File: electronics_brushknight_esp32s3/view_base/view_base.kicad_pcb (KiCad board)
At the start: 4 copper layers, 81.2 x 81.2 mm, 108 parts, among them J1 BLDC, J2 USB_C_Receptacle_USB2.0, J3 LCD, J4 A, J5 B, J6 LCD - FPC, Q1 MMBT4403, Q2 UMH3N, U1 MT6701-CT, U10 ESP32-S3-WROOM-1-N8R8, U2 CP2102N-A02-GQFN28, U4 HX711, U5 TMC6300, U7 SN74LV1T34DBV, U8 VEML7700, U9 TS1117BCW33_RPG

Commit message: re-routed things
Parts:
- removed D1, D2, D3, D4, D5, D6, D7, D8: SK6812SIDE-A, cleaned footprints:SK6812-SIDE-A
- removed H4: MountHole, Holes:MountingHole_2.2mm_M2_ISO7380_Pad_NonVirtual
- removed Q2: UMH3N, cleaned footprints:SOT-363_SC-70-6
- removed R22: 1K, cleaned footprints:R_0603_1608Metric
- added C100: 0.1uF, cleaned footprints:C_0402_1005Metric, F.Cu at (89.3, 122.8)
- added C101: 0.1uF, cleaned footprints:C_0402_1005Metric, F.Cu at (93.5, 124.3)
- added C11: 0.1uF, cleaned footprints:C_0402_1005Metric, F.Cu at (125.1, 97.8)
- added C30: 0.1uF, cleaned footprints:C_0402_1005Metric, F.Cu at (100.0, 125.2)
- added C31: 0.1uF, cleaned footprints:C_0402_1005Metric, F.Cu at (97.8, 74.9)
- added C32: 0.1uF, cleaned footprints:C_0402_1005Metric, F.Cu at (97.8, 125.1)
- added C33: 0.1uF, cleaned footprints:C_0402_1005Metric, F.Cu at (102.2, 74.9)
- added C34: 0.1uF, cleaned footprints:C_0402_1005Metric, F.Cu at (106.5, 124.3)
- added C35: 0.1uF, cleaned footprints:C_0402_1005Metric, F.Cu at (100.0, 74.8)
- added C36: 0.1uF, cleaned footprints:C_0402_1005Metric, F.Cu at (110.7, 122.9)
- added C37: 0.1uF, cleaned footprints:C_0402_1005Metric, F.Cu at (108.6, 76.3)
- added C38: 0.1uF, cleaned footprints:C_0402_1005Metric, F.Cu at (112.6, 78.2)
- added C39: 0.1uF, cleaned footprints:C_0402_1005Metric, F.Cu at (114.5, 120.7)
- added C40: 0.1uF, cleaned footprints:C_0402_1005Metric, F.Cu at (116.2, 80.7)
- added C41: 0.1uF, cleaned footprints:C_0402_1005Metric, F.Cu at (117.8, 117.8)
- added C42: 0.1uF, cleaned footprints:C_0402_1005Metric, F.Cu at (119.3, 83.8)
- added C43: 0.1uF, cleaned footprints:C_0402_1005Metric, F.Cu at (120.7, 114.5)
- added C44: 0.1uF, cleaned footprints:C_0402_1005Metric, F.Cu at (121.8, 87.4)
- added C45: 0.1uF, cleaned footprints:C_0402_1005Metric, F.Cu at (123.7, 91.4)
- added C46: 0.1uF, cleaned footprints:C_0402_1005Metric, F.Cu at (122.8, 110.7)
- added C47: 0.1uF, cleaned footprints:C_0402_1005Metric, F.Cu at (91.4, 76.3)
- added C48: 0.1uF, cleaned footprints:C_0402_1005Metric, F.Cu at (124.3, 106.5)
- added C49: 0.1uF, cleaned footprints:C_0402_1005Metric, F.Cu at (87.4, 78.2)
- added C50: 0.1uF, cleaned footprints:C_0402_1005Metric, F.Cu at (124.8, 104.4)
- added C51: 0.1uF, cleaned footprints:C_0402_1005Metric, F.Cu at (83.8, 80.7)
- added C52: 0.1uF, cleaned footprints:C_0402_1005Metric, F.Cu at (80.7, 83.8)
- added C53: 0.1uF, cleaned footprints:C_0402_1005Metric, F.Cu at (124.3, 93.5)
- added C54: 0.1uF, cleaned footprints:C_0402_1005Metric, F.Cu at (78.2, 87.4)
- added C55: 0.1uF, cleaned footprints:C_0402_1005Metric, F.Cu at (124.8, 95.6)
- added C56: 0.1uF, cleaned footprints:C_0402_1005Metric, F.Cu at (76.3, 91.4)
- added C57: 0.1uF, cleaned footprints:C_0402_1005Metric, F.Cu at (122.8, 89.3)
- added C58: 0.1uF, cleaned footprints:C_0402_1005Metric, F.Cu at (74.9, 97.8)
- added C59: 0.1uF, cleaned footprints:C_0402_1005Metric, F.Cu at (74.9, 102.2)
- added C60: 0.1uF, cleaned footprints:C_0402_1005Metric, F.Cu at (74.8, 100.0)
- added C61: 0.1uF, cleaned footprints:C_0402_1005Metric, F.Cu at (76.3, 108.6)
- added C62: 0.1uF, cleaned footprints:C_0402_1005Metric, F.Cu at (78.2, 112.6)
- added C63: 0.1uF, cleaned footprints:C_0402_1005Metric, F.Cu at (120.7, 85.5)
- added C64: 0.1uF, cleaned footprints:C_0402_1005Metric, F.Cu at (117.8, 82.2)
- added C65: 0.1uF, cleaned footprints:C_0402_1005Metric, F.Cu at (114.5, 79.3)
- added C66: 0.1uF, cleaned footprints:C_0402_1005Metric, F.Cu at (110.7, 77.2)
- added C67: 0.1uF, cleaned footprints:C_0402_1005Metric, F.Cu at (80.7, 116.2)
- added C68: 0.1uF, cleaned footprints:C_0402_1005Metric, F.Cu at (83.8, 119.3)
- added C69: 0.1uF, cleaned footprints:C_0402_1005Metric, F.Cu at (87.4, 121.8)
- added C70: 0.1uF, cleaned footprints:C_0402_1005Metric, F.Cu at (91.4, 123.7)
- added C71: 0.1uF, cleaned footprints:C_0402_1005Metric, F.Cu at (106.5, 75.6)
- added C72: 0.1uF, cleaned footprints:C_0402_1005Metric, F.Cu at (104.4, 75.2)
- added C73: 0.1uF, cleaned footprints:C_0402_1005Metric, F.Cu at (93.5, 75.6)
- added C74: 0.1uF, cleaned footprints:C_0402_1005Metric, F.Cu at (95.6, 75.2)
- added C75: 0.1uF, cleaned footprints:C_0402_1005Metric, F.Cu at (95.6, 124.8)
- added C76: 0.1uF, cleaned footprints:C_0402_1005Metric, F.Cu at (102.2, 125.1)
- added C77: 0.1uF, cleaned footprints:C_0402_1005Metric, F.Cu at (104.4, 124.8)
- added C79: 0.1uF, cleaned footprints:C_0402_1005Metric, F.Cu at (89.3, 77.2)
- added C80: 0.1uF, cleaned footprints:C_0402_1005Metric, F.Cu at (85.5, 79.4)
- added C81: 0.1uF, cleaned footprints:C_0402_1005Metric, F.Cu at (82.2, 82.2)
- added C82: 0.1uF, cleaned footprints:C_0402_1005Metric, F.Cu at (79.4, 85.5)
- added C88: 0.1uF, cleaned footprints:C_0402_1005Metric, F.Cu at (77.2, 89.3)
- added C90: 0.1uF, cleaned footprints:C_0402_1005Metric, F.Cu at (75.7, 93.5)
- added C92: 0.1uF, cleaned footprints:C_0402_1005Metric, F.Cu at (75.2, 95.6)
- added C94: 0.1uF, cleaned footprints:C_0402_1005Metric, F.Cu at (75.2, 104.4)
- added C95: 0.1uF, cleaned footprints:C_0402_1005Metric, F.Cu at (75.6, 106.5)
- added C96: 0.1uF, cleaned footprints:C_0402_1005Metric, F.Cu at (77.2, 110.7)
- added C97: 0.1uF, cleaned footprints:C_0402_1005Metric, F.Cu at (79.3, 114.5)
- added C98: 0.1uF, cleaned footprints:C_0402_1005Metric, F.Cu at (82.2, 117.8)
- added C99: 0.1uF, cleaned footprints:C_0402_1005Metric, F.Cu at (85.5, 120.6)
- added D10: SK6812, cleaned footprints:LED_SK6812_EC15_1.5x1.5mm, F.Cu at (97.7, 126.7)
- added D11: SK6812, cleaned footprints:LED_SK6812_EC15_1.5x1.5mm, F.Cu at (95.3, 126.3)
- added D12: SK6812, cleaned footprints:LED_SK6812_EC15_1.5x1.5mm, F.Cu at (93.1, 125.8)
- added D13: SK6812, cleaned footprints:LED_SK6812_EC15_1.5x1.5mm, F.Cu at (90.8, 125.1)
- added D14: SK6812, cleaned footprints:LED_SK6812_EC15_1.5x1.5mm, F.Cu at (88.7, 124.2)
- added D15: SK6812, cleaned footprints:LED_SK6812_EC15_1.5x1.5mm, F.Cu at (86.6, 123.2)
- added D16: SK6812, cleaned footprints:LED_SK6812_EC15_1.5x1.5mm, F.Cu at (84.7, 121.9)
- added D17: SK6812, cleaned footprints:LED_SK6812_EC15_1.5x1.5mm, F.Cu at (82.8, 120.5)
- added D18: SK6812, cleaned footprints:LED_SK6812_EC15_1.5x1.5mm, F.Cu at (81.1, 118.9)
- added D19: SK6812, cleaned footprints:LED_SK6812_EC15_1.5x1.5mm, F.Cu at (79.5, 117.2)
- added D20: SK6812, cleaned footprints:LED_SK6812_EC15_1.5x1.5mm, F.Cu at (78.1, 115.3)
- added D21: SK6812, cleaned footprints:LED_SK6812_EC15_1.5x1.5mm, F.Cu at (76.8, 113.4)
- added D22: SK6812, cleaned footprints:LED_SK6812_EC15_1.5x1.5mm, F.Cu at (75.8, 111.3)
- added D23: SK6812, cleaned footprints:LED_SK6812_EC15_1.5x1.5mm, F.Cu at (74.9, 109.2)
- added D24: SK6812, cleaned footprints:LED_SK6812_EC15_1.5x1.5mm, F.Cu at (74.2, 106.9)
- added D25: SK6812, cleaned footprints:LED_SK6812_EC15_1.5x1.5mm, F.Cu at (73.7, 104.6)
- added D26: SK6812, cleaned footprints:LED_SK6812_EC15_1.5x1.5mm, F.Cu at (73.4, 102.3)
- added D27: SK6812, cleaned footprints:LED_SK6812_EC15_1.5x1.5mm, F.Cu at (73.2, 100.0)
- added D28: SK6812, cleaned footprints:LED_SK6812_EC15_1.5x1.5mm, F.Cu at (73.4, 97.7)
- added D29: SK6812, cleaned footprints:LED_SK6812_EC15_1.5x1.5mm, F.Cu at (73.7, 95.4)
- added D30: SK6812, cleaned footprints:LED_SK6812_EC15_1.5x1.5mm, F.Cu at (74.2, 93.1)
- added D31: SK6812, cleaned footprints:LED_SK6812_EC15_1.5x1.5mm, F.Cu at (74.9, 90.9)
- added D32: SK6812, cleaned footprints:LED_SK6812_EC15_1.5x1.5mm, F.Cu at (75.8, 88.7)
- added D33: SK6812, cleaned footprints:LED_SK6812_EC15_1.5x1.5mm, F.Cu at (76.8, 86.6)
- added D34: SK6812, cleaned footprints:LED_SK6812_EC15_1.5x1.5mm, F.Cu at (78.1, 84.7)
- added D35: SK6812, cleaned footprints:LED_SK6812_EC15_1.5x1.5mm, F.Cu at (79.5, 82.8)
- added D36: SK6812, cleaned footprints:LED_SK6812_EC15_1.5x1.5mm, F.Cu at (81.1, 81.1)
- added D37: SK6812, cleaned footprints:LED_SK6812_EC15_1.5x1.5mm, F.Cu at (82.8, 79.5)
- added D38: SK6812, cleaned footprints:LED_SK6812_EC15_1.5x1.5mm, F.Cu at (84.7, 78.1)
- added D39: SK6812, cleaned footprints:LED_SK6812_EC15_1.5x1.5mm, F.Cu at (86.6, 76.8)
- added D40: SK6812, cleaned footprints:LED_SK6812_EC15_1.5x1.5mm, F.Cu at (88.7, 75.8)
- added D41: SK6812, cleaned footprints:LED_SK6812_EC15_1.5x1.5mm, F.Cu at (90.8, 74.9)
- added D42: SK6812, cleaned footprints:LED_SK6812_EC15_1.5x1.5mm, F.Cu at (109.2, 74.9)
- added D43: SK6812, cleaned footprints:LED_SK6812_EC15_1.5x1.5mm, F.Cu at (123.2, 86.6)
- added D44: SK6812, cleaned footprints:LED_SK6812_EC15_1.5x1.5mm, F.Cu at (126.3, 104.6)
- added D45: SK6812, cleaned footprints:LED_SK6812_EC15_1.5x1.5mm, F.Cu at (93.1, 74.2)
- added D46: SK6812, cleaned footprints:LED_SK6812_EC15_1.5x1.5mm, F.Cu at (111.3, 75.8)
- added D47: SK6812, cleaned footprints:LED_SK6812_EC15_1.5x1.5mm, F.Cu at (124.2, 88.7)
- added D48: SK6812, cleaned footprints:LED_SK6812_EC15_1.5x1.5mm, F.Cu at (125.8, 106.9)
- added D49: SK6812, cleaned footprints:LED_SK6812_EC15_1.5x1.5mm, F.Cu at (95.4, 73.7)
- added D50: SK6812, cleaned footprints:LED_SK6812_EC15_1.5x1.5mm, F.Cu at (113.4, 76.8)
- added D51: SK6812, cleaned footprints:LED_SK6812_EC15_1.5x1.5mm, F.Cu at (125.1, 90.9)
- added D52: SK6812, cleaned footprints:LED_SK6812_EC15_1.5x1.5mm, F.Cu at (125.1, 109.2)
- added D53: SK6812, cleaned footprints:LED_SK6812_EC15_1.5x1.5mm, F.Cu at (97.7, 73.4)
- added D54: SK6812, cleaned footprints:LED_SK6812_EC15_1.5x1.5mm, F.Cu at (115.3, 78.1)
- added D55: SK6812, cleaned footprints:LED_SK6812_EC15_1.5x1.5mm, F.Cu at (125.8, 93.1)
- added D56: SK6812, cleaned footprints:LED_SK6812_EC15_1.5x1.5mm, F.Cu at (124.2, 111.3)
- added D57: SK6812, cleaned footprints:LED_SK6812_EC15_1.5x1.5mm, F.Cu at (100.0, 73.2)
- added D58: SK6812, cleaned footprints:LED_SK6812_EC15_1.5x1.5mm, F.Cu at (117.2, 79.5)
- added D59: SK6812, cleaned footprints:LED_SK6812_EC15_1.5x1.5mm, F.Cu at (126.3, 95.4)
- added D60: SK6812, cleaned footprints:LED_SK6812_EC15_1.5x1.5mm, F.Cu at (123.2, 113.4)
- added D61: SK6812, cleaned footprints:LED_SK6812_EC15_1.5x1.5mm, F.Cu at (102.3, 73.4)
- added D62: SK6812, cleaned footprints:LED_SK6812_EC15_1.5x1.5mm, F.Cu at (118.9, 81.1)
- added D63: SK6812, cleaned footprints:LED_SK6812_EC15_1.5x1.5mm, F.Cu at (126.6, 97.7)
- added D64: SK6812, cleaned footprints:LED_SK6812_EC15_1.5x1.5mm, F.Cu at (121.9, 115.3)
- added D65: SK6812, cleaned footprints:LED_SK6812_EC15_1.5x1.5mm, F.Cu at (104.7, 73.7)
- added D66: SK6812, cleaned footprints:LED_SK6812_EC15_1.5x1.5mm, F.Cu at (120.5, 82.8)
- added D67: SK6812, cleaned footprints:LED_SK6812_EC15_1.5x1.5mm, F.Cu at (126.7, 100.0)
- added D68: SK6812, cleaned footprints:LED_SK6812_EC15_1.5x1.5mm, F.Cu at (120.5, 117.2)
- added D69: SK6812, cleaned footprints:LED_SK6812_EC15_1.5x1.5mm, F.Cu at (106.9, 74.2)
- added D70: SK6812, cleaned footprints:LED_SK6812_EC15_1.5x1.5mm, F.Cu at (121.9, 84.7)
- added D71: SK6812, cleaned footprints:LED_SK6812_EC15_1.5x1.5mm, F.Cu at (126.7, 102.3)
- added D72: SK6812, cleaned footprints:LED_SK6812_EC15_1.5x1.5mm, F.Cu at (118.9, 118.9)
- added D73: SK6812, cleaned footprints:LED_SK6812_EC15_1.5x1.5mm, F.Cu at (117.2, 120.5)
- added D74: SK6812, cleaned footprints:LED_SK6812_EC15_1.5x1.5mm, F.Cu at (115.3, 121.9)
- added D75: SK6812, cleaned footprints:LED_SK6812_EC15_1.5x1.5mm, F.Cu at (113.4, 123.2)
- added D76: SK6812, cleaned footprints:LED_SK6812_EC15_1.5x1.5mm, F.Cu at (111.3, 124.2)
- added D77: SK6812, cleaned footprints:LED_SK6812_EC15_1.5x1.5mm, F.Cu at (109.1, 125.1)
- added D78: SK6812, cleaned footprints:LED_SK6812_EC15_1.5x1.5mm, F.Cu at (106.9, 125.8)
- added D79: SK6812, cleaned footprints:LED_SK6812_EC15_1.5x1.5mm, F.Cu at (104.7, 126.3)
- added D80: SK6812, cleaned footprints:LED_SK6812_EC15_1.5x1.5mm, F.Cu at (102.3, 126.7)
- added D9: SK6812, cleaned footprints:LED_SK6812_EC15_1.5x1.5mm, F.Cu at (100.0, 126.8)
- added REF**: fpc_wire_hole_6mm, view_custom:fpc_wire_hole_6mm, F.Cu at (97.2, 102.8)
- C1, C2, C29, C3, C4, C5, C6, C7, C8: footprint cleaned footprints:C_0603_1608Metric -> cleaned footprints:C_0402_1005Metric
- TP1, TP10, TP11, TP12, TP13, TP14, TP15, TP16, TP3, TP4, TP5, TP6, TP7, TP8, TP9: footprint Modified:TestPoint_Pad_D2.0mm_ValueSilk -> cleaned footprints:TestPoint_Pad_D2.0mm_ValueSilk
- TP2: value 3.3v -> 3V3; footprint Modified:TestPoint_Pad_D2.0mm_ValueSilk -> cleaned footprints:TestPoint_Pad_D2.0mm_ValueSilk
- U2: value CP2102N-A02-GQFN28 -> USBLC6-2SC6; footprint cp2102:Silicon_Labs-CP2102N-A02-GQFN28-IPC_A -> Package_TO_SOT_SMD:SOT-23-6
- moved C8 41.1 mm to (125.1, 102.2), turned to 85 degrees
- moved C7 38.1 mm to (125.2, 100.0), turned to 90 degrees
- moved U7 34.0 mm to (89.6, 136.8)
- moved C29 33.9 mm to (89.6, 134.4), turned to 180 degrees
- moved TP12 29.8 mm to (81.8, 138.2)
- moved C1 26.3 mm to (108.6, 123.7), turned to 20 degrees
- moved C6 26.3 mm to (123.7, 108.6), turned to 70 degrees
- moved TP15 25.8 mm to (65.8, 138.2)
- moved C2 24.2 mm to (112.6, 121.8), turned to 30 degrees
- moved C5 24.2 mm to (121.8, 112.6), turned to 60 degrees
- moved TP14 18.0 mm to (73.8, 138.2), turned to 180 degrees
- moved TP16 14.5 mm to (69.8, 138.2)
- moved TP9 12.7 mm to (67.5, 104.5)
- moved R15 8.63 mm to (67.2, 116.2), turned to -90 degrees
- moved R16 8.63 mm to (68.8, 116.2), turned to 90 degrees
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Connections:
- R13 pad 2: /SDA -> SDA
- R14 pad 2: /SCL -> SCL
- TP4 pad 1: /SDA -> SDA
- TP5 pad 1: /SCL -> SCL
- U10 pad 10: /TMC_VL -> /TMC_WH
- U10 pad 11: /TMC_WL -> /TMC_VH
- U10 pad 12: /SCL -> /TMC_UH
- U10 pad 13: /TMC_UL -> /ESP_USB_D-
- U10 pad 14: /TMC_UH -> /ESP_USB_D+
- U10 pad 18: unconnected-(U10-IO10-Pad18) -> /LCD_RST
- U10 pad 19: unconnected-(U10-IO11-Pad19) -> /MAG_CSN
- U10 pad 20: /TMC_WH -> /LED_DATA_3V3
- U10 pad 22: /MAG_CSN -> /MAG_DO
- U10 pad 23: /TMC_VH -> /STRAIN_DO
- U10 pad 29: /TMC_DIAG -> unconnected-(U10-IO36-Pad29)
- U10 pad 30: /MAG_DO -> unconnected-(U10-IO37-Pad30)
- U10 pad 31: /STRAIN_DO -> SCL
- U10 pad 32: unconnected-(U10-IO39-Pad32) -> SDA
- U10 pad 6: /LCD_RST -> /TMC_DIAG
- U10 pad 7: /LED_DATA_3V3 -> /TMC_VL
- U10 pad 8: /SDA -> /TMC_WL
- U10 pad 9: unconnected-(U10-IO16-Pad9) -> /TMC_UL
- U2 pad 1: unconnected-(U2-DCD-Pad1) -> /USB_D-
- U2 pad 2: unconnected-(U2-~{RI}/CLK-Pad2) -> GND
- U2 pad 3: GND -> /USB_D+
- U2 pad 4: /USB_D+ -> /ESP_USB_D+
- U2 pad 5: /USB_D- -> +5V
- U2 pad 6: +3V3 -> /ESP_USB_D-
- U8 pad 1: /SCL -> SCL
- U8 pad 4: /SDA -> SDA
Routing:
- net /SCL: track 139.1 -> 0.00 mm, vias 3 -> 0
- net SCL: track 0.00 -> 129.3 mm, vias 0 -> 2
- net /SDA: track 128.4 -> 0.00 mm, vias 3 -> 0
- net SDA: track 0.00 -> 115.8 mm, vias 0 -> 2
- net /USB_SERIAL_RXI: track 41.5 -> 9.54 mm
- net /USB_SERIAL_TXO: track 43.5 -> 14.0 mm
- net /ESP32_BOOT: track 56.0 -> 27.7 mm, vias 3 -> 2
- net Net-(D4-DOUT): track 26.0 -> 0.00 mm
- net Net-(D6-DOUT): track 26.0 -> 0.00 mm
- net /MAG_DO: track 79.4 -> 54.0 mm, vias 3 -> 2
- net Net-(D2-DOUT): track 25.3 -> 0.00 mm, vias 2 -> 0
- net /LCD_SCK: track 17.4 -> 40.1 mm, vias 1 -> 2
- net /LCD_CMD: track 7.75 -> 29.7 mm
- net /TMC_DIAG: track 109.5 -> 87.5 mm
- net /LCD_CS: track 23.3 -> 44.3 mm
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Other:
- outline, holes or cut-outs redrawn
- board text added: "SmartKnob DevKit"
- board text added: "esp32s3"
- board text removed: "Base PCB esp32s3"
- board text removed: "SmartKnob View"
- board text removed: "power"

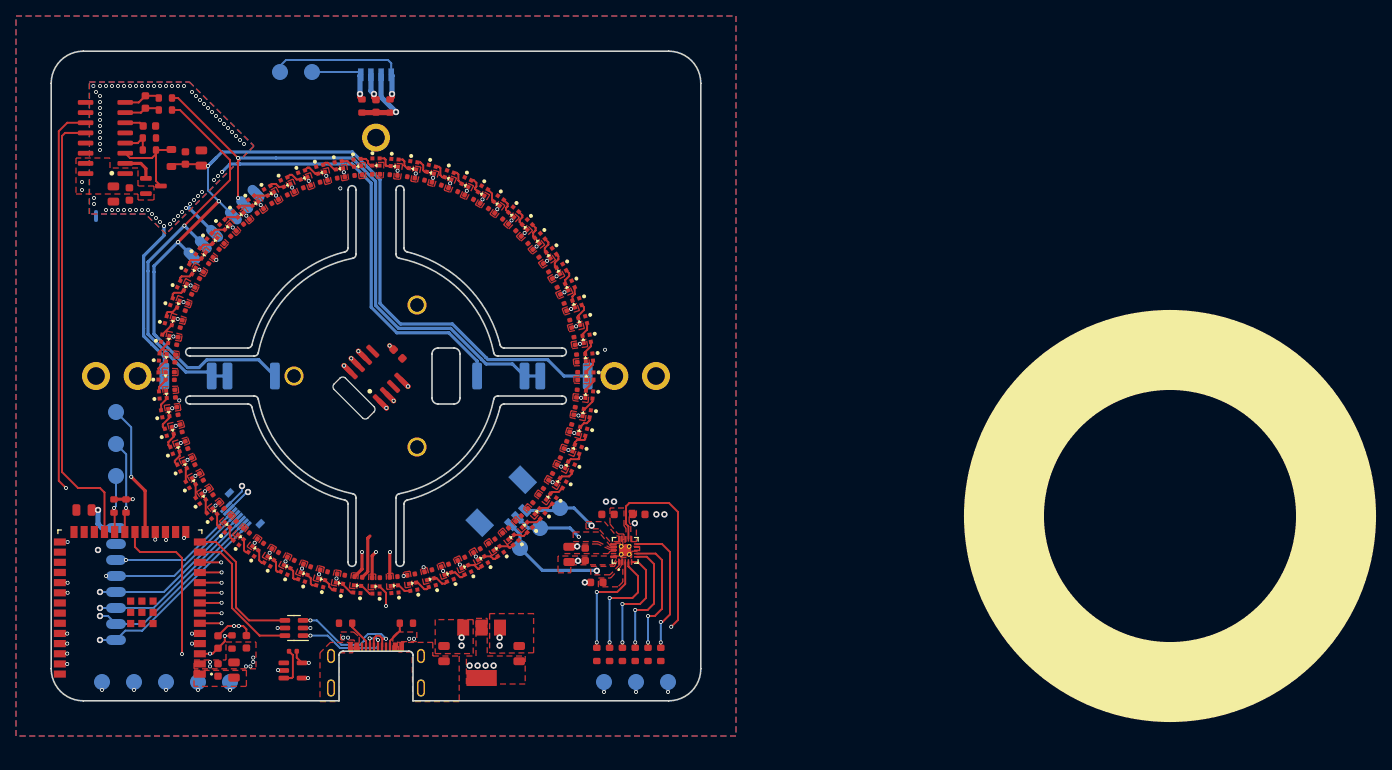
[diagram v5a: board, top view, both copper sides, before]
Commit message: updated screen PCB
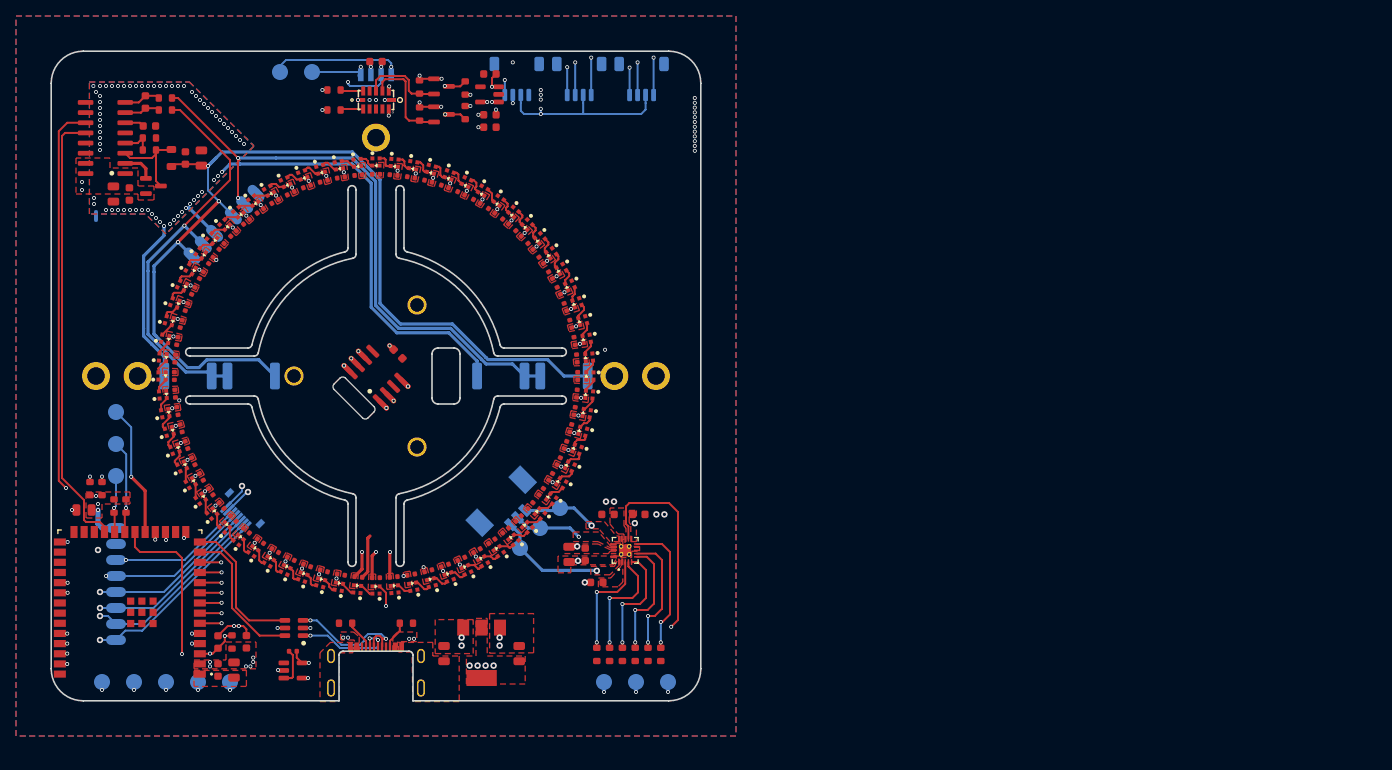
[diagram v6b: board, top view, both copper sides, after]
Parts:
- added C78: 10uF, smd_clean:C_0603_1608Metric, F.Cu at (114.2, 62.2)
- added C83: 10uF, smd_clean:C_0603_1608Metric, F.Cu at (114.2, 67.3)
- added C84: 100nF, smd_clean:C_0603_1608Metric, F.Cu at (114.2, 68.9)
- added J7: Conn_01x04_Socket, cleaned footprints:JST_SH_SM04B-SRSS-TB_1x04-1MP_P1.00mm_Horizontal, B.Cu at (133.2, 62.9)
- added J8: Conn_01x04_Socket, cleaned footprints:JST_SH_SM04B-SRSS-TB_1x04-1MP_P1.00mm_Horizontal, B.Cu at (125.4, 62.9)
- added J9: Conn_01x04_Socket, cleaned footprints:JST_SH_SM04B-SRSS-TB_1x04-1MP_P1.00mm_Horizontal, B.Cu at (117.6, 62.9)
- added Q2: BSS138, smd_clean:SOT-23, F.Cu at (108.2, 67.3)
- added Q3: BSS138, smd_clean:SOT-23, F.Cu at (108.2, 63.8)
- added R22: 10K, smd_clean:R_0603_1608Metric, F.Cu at (94.8, 66.8)
- added R23: 10K, smd_clean:R_0603_1608Metric, F.Cu at (105.5, 67.2)
- added R24: 10K, smd_clean:R_0603_1608Metric, F.Cu at (105.4, 63.9)
- added R25: 10K, smd_clean:R_0603_1608Metric, F.Cu at (94.8, 64.2)
- added R26: 10K, smd_clean:R_0603_1608Metric, F.Cu at (111.2, 67.1)
- added R27: 10K, smd_clean:R_0603_1608Metric, F.Cu at (111.2, 64.0)
- added U3: VL53L0CXV0DH_1, smd_clean:LGA12_1, F.Cu at (100.0, 65.5)
- added U6: LP5907MFX-2.8, cleaned footprints:SOT-23-5, F.Cu at (114.2, 64.8)
- U2: footprint Package_TO_SOT_SMD:SOT-23-6 -> smd_clean:SOT-23-6
- moved Z5 83.7 mm to (40.8, 40.8)
- moved R14 60.8 mm to (64.2, 114.1)
- moved R13 57.8 mm to (65.8, 114.1)
- moved C27 5.55 mm to (100.0, 60.7), turned to 180 degrees
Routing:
- net SDA: track 115.8 -> 183.2 mm, vias 2 -> 8
- net SCL: track 129.3 -> 190.9 mm, vias 2 -> 7
- net +5V: track 20.8 -> 43.7 mm, vias 69 -> 70
- net SCL_2.8: track 0.00 -> 12.6 mm
- net SDA_2.8: track 0.00 -> 10.5 mm
- net +2V8: track 0.00 -> 10.1 mm, vias 0 -> 11
- net GND: track 24.4 -> 32.1 mm, vias 17 -> 40
- net Net-(U3-XSHUT): track 0.00 -> 2.88 mm
- net Net-(U3-GPIO1): track 0.00 -> 2.88 mm
- net /STRAIN_DO: track 56.4 -> 55.8 mm
- net +3V3: track 59.7 -> 59.8 mm, vias 21 -> 27
- added copper zone on In2.Cu, net +2V8
- added copper zone on In1.Cu, net GND
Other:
- board text added: "5"
- board text added: "G"
- board text added: "G - Ground 5 - VCC 5V D - SDA C - SCL"
- board text removed: "DATE: ${COMMIT_DATE_LONG} COMMIT: ${COMMIT_HASH}"
